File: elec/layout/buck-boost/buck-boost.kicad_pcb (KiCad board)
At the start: 6 copper layers, 69 parts, among them U10 2.49kΩ ±1% 62.5mW, U11 4.7µF ±10% 100V X7R, U12 4.7µF ±10% 100V X7R, U13 4.7µF ±10% 100V X7R, U14 10µF ±10% 100V X7S, U15 10µF ±10% 100V X7S, U16 10µF ±10% 100V X7S, U17 10µF ±10% 100V X7S, U18 1µF ±10% 100V X7R, U19 100nF ±10% 100V X7R, U2 100nF ±10% 50V X7R, U20 100pF ±5% 100V C0G, U21 470nF ±20% 16V X5R, U22 100nF ±10% 16V X7R, U23 10Ω ±1% 62.5mW, U24 100nF ±10% 16V X7R, U25 10Ω ±1% 62.5mW, U26 5mΩ ±1% 1W, U27 4.7µF ±10% 100V X7R, U28 4.7µF ±10% 100V X7R, U29 4.7µF ±10% 100V X7R, U3 100nF ±10% 50V X7R, U30 10µF ±10% 100V X7S, U31 10µF ±10% 100V X7S, U32 10µF ±10% 100V X7S, U33 10µF ±10% 100V X7S, U34 1µF ±10% 100V X7R, U35 100nF ±10% 100V X7R, U36 100pF ±5% 100V C0G, U37 470nF ±20% 16V X5R, U38 100nF ±10% 16V X7R, U39 10Ω ±1% 62.5mW, U4 50kΩ ±1% 62.5mW, U40 100nF ±10% 16V X7R, U41 10Ω ±1% 62.5mW, U42 5mΩ ±1% 1W, U43 13.7kΩ ±1% 62.5mW, U44 249kΩ ±1% 100mW, U45 1MΩ ±1% 100mW, U46 133kΩ ±1% 100mW, U47 25.5kΩ ±0% 100mW, U48 4.7µF ±10% 25V X5R, U49 100nF ±10% 100V X7R, U50 1µF ±10% 250V X7R, U51 4.7µF ±10% 100V X7R, U52 4.7µF ±10% 100V X7R, U54 0Ω 62.5mW, U58 30.1kΩ ±1% 62.5mW, U59 5.23kΩ ±1% 100mW, U9 4.7µF ±10% 25V X5R

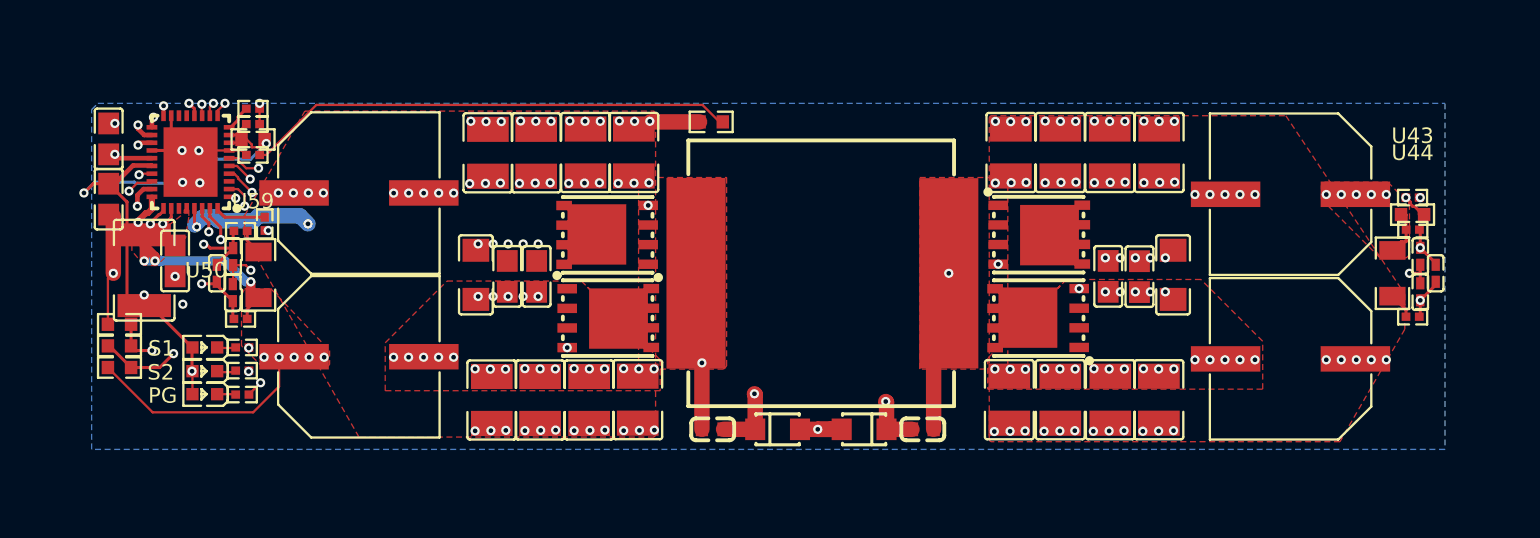
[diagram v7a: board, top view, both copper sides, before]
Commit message: Fix address bit issue, update layouts
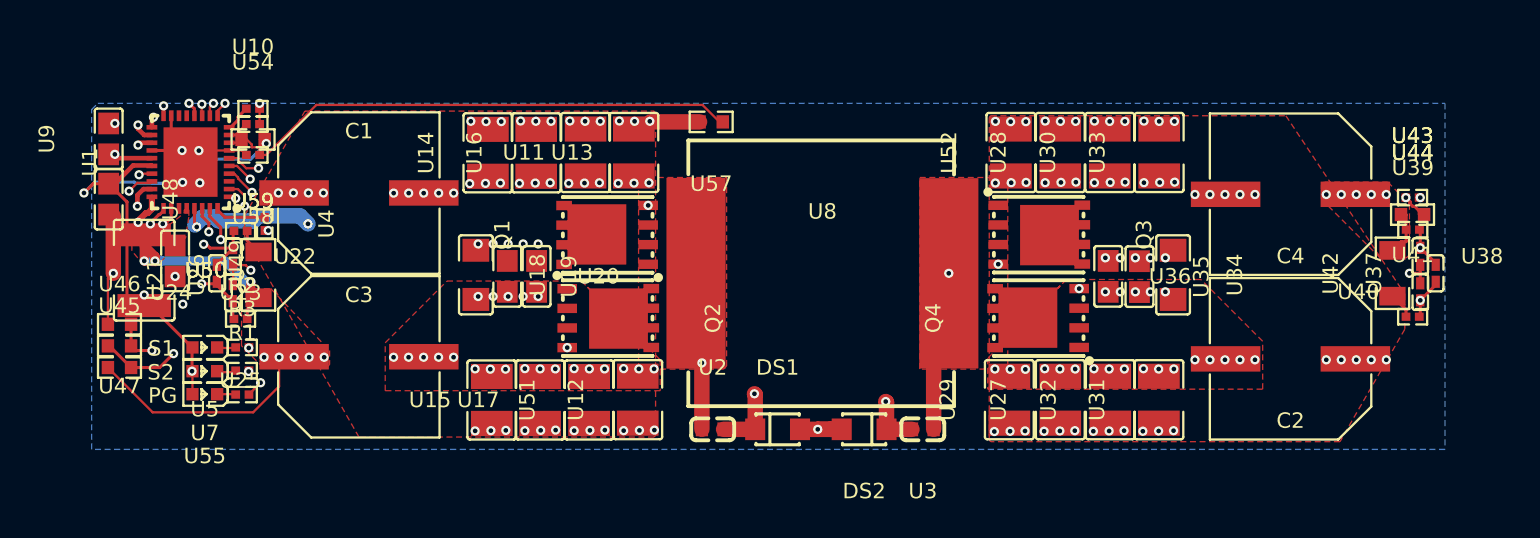
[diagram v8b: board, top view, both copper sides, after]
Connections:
- C1 pad 1: hv -> hv-1
- C1 pad 2: gnd -> gnd-3
- C2 pad 1: hv-1 -> hv-2
- C2 pad 2: gnd -> gnd-3
- C3 pad 2: gnd -> gnd-3
- C4 pad 1: hv-2 -> hv
- C4 pad 2: gnd -> gnd-3
- DS1 pad 2: anode-1 -> anode
- DS2 pad 2: anode-1 -> anode
- Q1 pad 1: source -> line-6
- Q1 pad 2: source -> line-6
- Q1 pad 3: source -> line-6
- Q1 pad 4: line -> line-1
- Q1 pad 5: hv -> hv-1
- Q1 pad 6: hv -> hv-1
- Q1 pad 7: hv -> hv-1
- Q1 pad 8: hv -> hv-1
- Q2 pad 1: gnd -> gnd-3
- Q2 pad 2: gnd -> gnd-3
- Q2 pad 3: gnd -> gnd-3
- Q2 pad 4: line-2 -> line
- Q2 pad 5: source -> line-6
- Q2 pad 6: source -> line-6
- Q2 pad 7: source -> line-6
- Q2 pad 8: source -> line-6
- Q3 pad 1: drain -> line-5
- Q3 pad 2: drain -> line-5
- Q3 pad 3: drain -> line-5
- Q3 pad 4: line-6 -> line-9
- Q3 pad 5: hv-1 -> hv-2
- Q3 pad 6: hv-1 -> hv-2
- Q3 pad 7: hv-1 -> hv-2
- Q3 pad 8: hv-1 -> hv-2
- Q4 pad 1: gnd -> gnd-3
- Q4 pad 2: gnd -> gnd-3
- Q4 pad 3: gnd -> gnd-3
- Q4 pad 4: gate -> line-3
- Q4 pad 5: drain -> line-5
- Q4 pad 6: drain -> line-5
- Q4 pad 7: drain -> line-5
- Q4 pad 8: drain -> line-5
- R1 pad 2: gnd-2 -> gnd-4
- R2 pad 2: gnd-3 -> gnd-2
- R3 pad 2: gnd-4 -> gnd
- U1 pad 13: line-3 -> line-4
- U1 pad 14: line-1 -> line-8
- U1 pad 17: gnd -> gnd-3
- U1 pad 18: drain -> line-5
- U1 pad 19: line-6 -> line-9
- U1 pad 21: gate -> line-3
- U1 pad 22: gnd -> gnd-3
- U1 pad 23: anode-1 -> anode
- U1 pad 24: anode -> anode-1
- U1 pad 25: line-2 -> line
- U1 pad 27: line -> line-1
- U1 pad 28: source -> line-6
- U1 pad 29: line-4 -> line-7
- U1 pad 30: line-5 -> line-2
- U1 pad 33: hv-2 -> hv
- U1 pad 37: gnd -> gnd-3
- U1 pad 4: gnd-3 -> gnd-2
- U1 pad 5: gnd-4 -> gnd
- U1 pad 6: gnd-2 -> gnd-4
- U1 pad 7: gnd -> gnd-3
- U10 pad 2: gnd -> gnd-3
- U11 pad 1: hv -> hv-1
- U11 pad 2: gnd -> gnd-3
- U12 pad 1: hv -> hv-1
- U12 pad 2: gnd -> gnd-3
- U13 pad 1: hv -> hv-1
- U13 pad 2: gnd -> gnd-3
- U14 pad 1: hv -> hv-1
- U14 pad 2: gnd -> gnd-3
- U15 pad 1: hv -> hv-1
- U15 pad 2: gnd -> gnd-3
- U16 pad 1: hv -> hv-1
- U16 pad 2: gnd -> gnd-3
- U17 pad 1: hv -> hv-1
- U17 pad 2: gnd -> gnd-3
- U18 pad 1: hv -> hv-1
- U18 pad 2: gnd -> gnd-3
- U19 pad 1: hv -> hv-1
- U19 pad 2: gnd -> gnd-3
- U2 pad 1: source -> line-6
- U20 pad 1: hv -> hv-1
- U20 pad 2: gnd -> gnd-3
- U21 pad 1: line-5 -> line-2
- U21 pad 2: line-4 -> line-7
- U22 pad 1: line-4 -> line-7
- U22 pad 2: gnd -> gnd-3
- U23 pad 1: hv -> hv-1
- U23 pad 2: line-4 -> line-7
- U24 pad 1: line-5 -> line-2
- U24 pad 2: gnd -> gnd-3
- U25 pad 2: line-5 -> line-2
- U26 pad 2: hv -> hv-1
- U27 pad 1: hv-1 -> hv-2
- U27 pad 2: gnd -> gnd-3
- U28 pad 1: hv-1 -> hv-2
- U28 pad 2: gnd -> gnd-3
- U29 pad 1: hv-1 -> hv-2
- U29 pad 2: gnd -> gnd-3
- U3 pad 1: drain -> line-5
- U30 pad 1: hv-1 -> hv-2
- U30 pad 2: gnd -> gnd-3
- U31 pad 1: hv-1 -> hv-2
- U31 pad 2: gnd -> gnd-3
- U32 pad 1: hv-1 -> hv-2
- U32 pad 2: gnd -> gnd-3
- U33 pad 1: hv-1 -> hv-2
- U33 pad 2: gnd -> gnd-3
- U34 pad 1: hv-1 -> hv-2
- U34 pad 2: gnd -> gnd-3
- U35 pad 1: hv-1 -> hv-2
- U35 pad 2: gnd -> gnd-3
- U36 pad 1: hv-1 -> hv-2
- U36 pad 2: gnd -> gnd-3
- U37 pad 1: line-1 -> line-8
- U37 pad 2: line-3 -> line-4
- U38 pad 1: line-3 -> line-4
- U38 pad 2: gnd -> gnd-3
- U39 pad 1: hv-2 -> hv
- U39 pad 2: line-3 -> line-4
- U4 pad 2: gnd -> gnd-3
- U40 pad 1: line-1 -> line-8
- U40 pad 2: gnd -> gnd-3
- U41 pad 1: hv-1 -> hv-2
- U41 pad 2: line-1 -> line-8
- U42 pad 1: hv-1 -> hv-2
- U42 pad 2: hv-2 -> hv
- U43 pad 2: gnd-1 -> output_v_sense-gnd
- U44 pad 1: hv-2 -> hv
- U47 pad 2: gnd -> gnd-3
- U48 pad 1: anode -> anode-1
- U48 pad 2: gnd -> gnd-3
- U49 pad 2: gnd -> gnd-3
- U5 pad 2: anode -> anode-1
- U50 pad 2: gnd -> gnd-3
- U51 pad 1: hv -> hv-1
- U51 pad 2: gnd -> gnd-3
- U52 pad 1: hv-1 -> hv-2
- U52 pad 2: gnd -> gnd-3
- U54 pad 2: gnd -> gnd-3
- U55 pad 2: anode -> anode-1
- U57 pad 2: gnd -> gnd-3
- U58 pad 2: gnd -> gnd-3
- U59 pad 1: anode -> anode-1
- U7 pad 2: anode -> anode-1
- U8 pad 1: source -> line-6
- U8 pad 2: drain -> line-5
- U9 pad 1: anode-1 -> anode
- U9 pad 2: gnd -> gnd-3
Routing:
- net line-8: track 0.00 -> 88.9 mm, vias 0 -> 2
- net hv: track 1.67 -> 78.8 mm, vias 33 -> 7
- net hv-2: track 78.8 -> 1.69 mm, vias 7 -> 34
- net line-4: track 10.5 -> 86.4 mm
- net drain: track 68.3 -> 0.00 mm, vias 2 -> 0
- net gate: track 67.3 -> 0.00 mm, vias 2 -> 0
- net line-9: track 0.00 -> 59.3 mm, vias 0 -> 2
- net line-5: track 10.1 -> 68.3 mm
- net source: track 55.2 -> 0.00 mm, vias 3 -> 0
- net line-1: track 88.9 -> 37.8 mm
- net anode-1: track 70.3 -> 35.4 mm, vias 2 -> 3
- net anode: track 35.4 -> 70.3 mm, vias 3 -> 2
- net line-2: track 38.0 -> 10.1 mm
- net line-3: track 86.4 -> 67.3 mm
- net gnd-3: track 12.5 -> 24.6 mm, vias 2 -> 90
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- added copper zone on B.Cu, net gnd-3
- added copper zone on F.Cu, net gnd-3
- added copper zone on In1.Cu, net gnd-3
- added copper zone on In2.Cu, net hv-2
- added copper zone on F.Cu, net line-5
- added copper zone on F.Cu, net line-6
- removed copper zone on F.Cu, net drain
- removed copper zone on B.Cu, net gnd
- removed copper zone on F.Cu, net gnd
- removed copper zone on In1.Cu, net gnd
- removed copper zone on In2.Cu, net hv
- removed copper zone on F.Cu, net source
